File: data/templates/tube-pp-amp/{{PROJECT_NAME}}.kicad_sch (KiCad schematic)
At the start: 22 parts, among them X1 6N2P, X2 6N2P, X3 6P14P, X4 6P14P, X5 OPT_PP_6K6_8

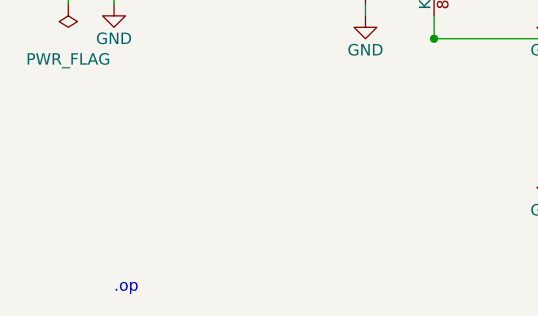
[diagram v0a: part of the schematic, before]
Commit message: T187 Phase 1: domain + facade snap-on-write entry-point
Domain (src/domain/grid.py):
- snap_to_grid(value, grid_mm=1.27) pure function; idempotent, FP-stable
- GridStepMm semantic alias
- OffGridEndpoint / OffGridReport frozen pydantic VO
- OffGridPositionError for EFACTORY_STRICT_GRID=1 strict mode

Facade (adapters/outbound/schematic_kicad/facade.py):
- _to_position now snaps both tuple-input and Position-input (idempotent
  for already-on-grid). Catches the edge-case where builder constructs
  Position(x_mm=..., y_mm=...) directly with off-grid coords (e.g. wire
  endpoint in bjt-ce-nfb at y=96.19 — root cause of disconnect after
  snap moved R_E to y=96.52).
- connect() snaps its Position start/end via _to_position too. Manhattan
  corner inherits snapped coords.
- _snap_position helper: silent snap by default; EFACTORY_STRICT_GRID=1
  raises OffGridPositionError for real off-grid drift (>1e-6 mm), FP
  jitter always silently snapped.
- name param plumbed through all add_* / junction / no_connect / label
  / spice_directive callsites for diagnostic error messages.
- add_ground / add_pwr_flag restructured to resolve reference before
  _to_position (so error carries real ref, not '<unknown>').

Templates regenerated (8 buildered via existing _BAKERS):
- se-amp, nfb-se-amp, op-amp-inverting, bjt-ce-nfb, tube-pp-amp,
  tube-line-preamp, tube-phono-riaa, active-lpf-sallen-key
- ERC check: 0 endpoint_off_grid warnings, 0 errors for all 8.
- 3 T031 builderless templates (6p13s/6zh32p/6zh38p) still dirty;
  fixed in Phase 4 via reverse-engineered builder.

Tests:
- New tests/unit/domain/test_grid.py (20 cases): snap correctness +
  idempotence + FP-jitter + custom grid + frozen VO + strict-mode error.
- New T187 cases in test_schematic_facade.py: silent snap default,
  strict-mode raise, FP-jitter tolerance, label/spice/ground/pwr_flag
  snap paths.
- Updated existing tests with off-grid literal coords (100→101.6,
  50→50.8 etc.) to articulate the new on-grid invariant.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
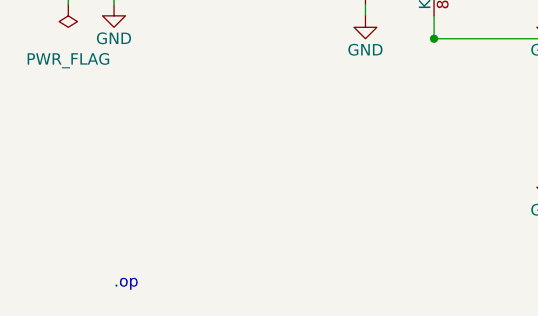
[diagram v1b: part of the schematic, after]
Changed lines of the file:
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@@
 	(text ".op"
 		(exclude_from_sim no)
-		(at 50.8 130 0)
+		(at 50.8 129.54 0)
 		(effects
 			(font
